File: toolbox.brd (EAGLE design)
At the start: 69.8 x 45 mm, 81 parts, among them IC1 PIC18F4XK22PT, IC3 78L05SMD, T1 BC847, U2 AD654JRZ, U3 ADUM7441ARQZ

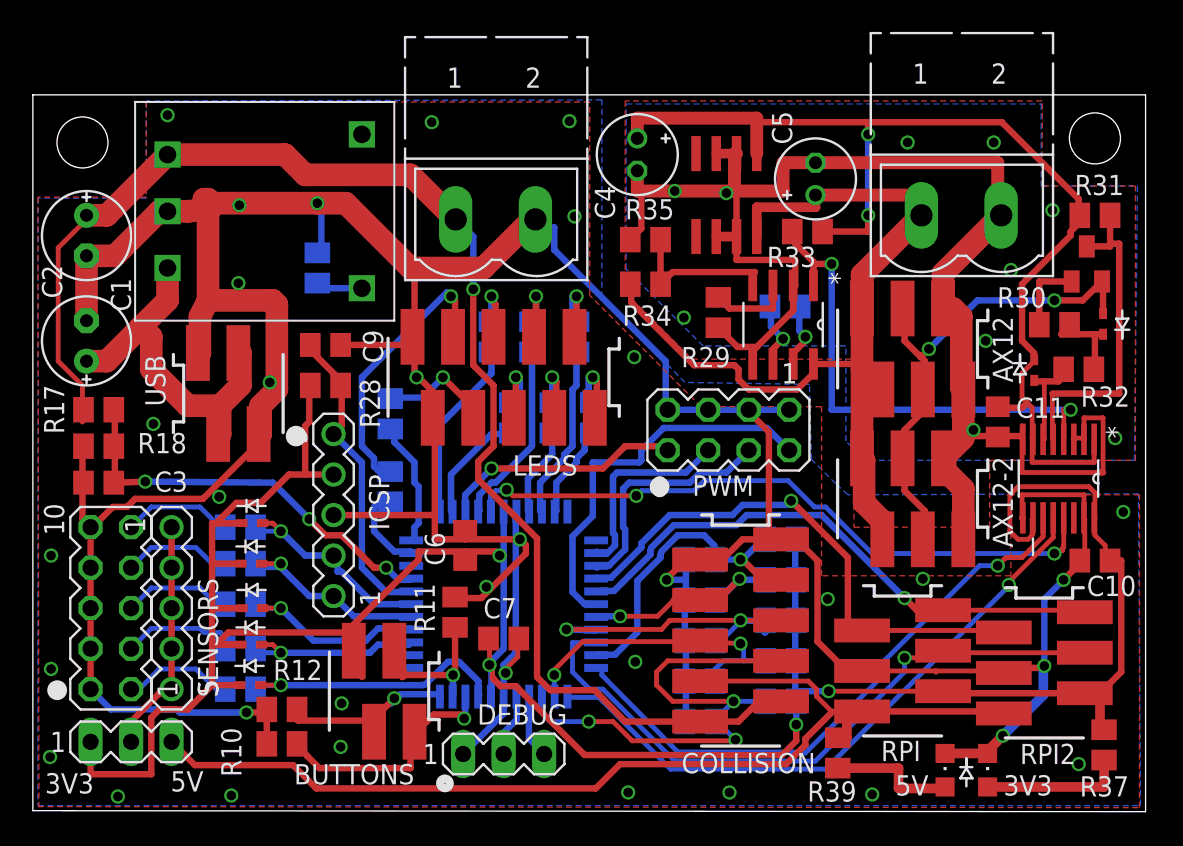
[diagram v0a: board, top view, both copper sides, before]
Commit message: added clipping circuit for collision sensors
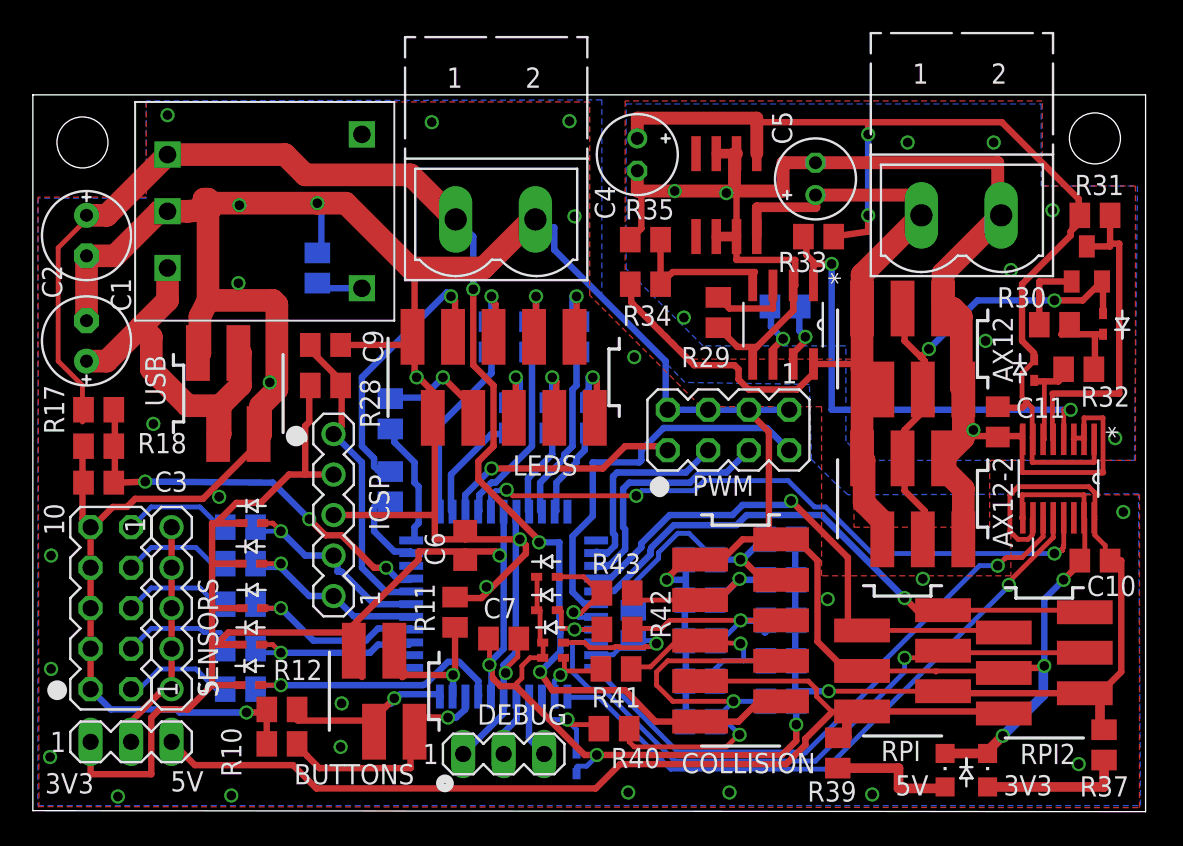
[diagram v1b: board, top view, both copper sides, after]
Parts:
- added D10, D11, D12, D8, D9: (no value), diode:SOD523
- added R40, R41, R42, R43, R44: 1k, rcl:M0805
- moved R33 0.77 mm to (49.3, 36.0)
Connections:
- new net N$66: D12.A, IC1.43, R44.1
- new net N$67: D8.A, IC1.3, R40.1
- new net N$69: D9.A, IC1.2, R41.1
- new net N$70: D10.A, IC1.41, R42.1
- new net N$71: D11.A, IC1.40, R43.1
- net N$41: now also R40.2; no longer IC1.3
- net N$42: now also R41.2; no longer IC1.2
- net N$43: now also R42.2; no longer IC1.41
- net N$44: now also R43.2; no longer IC1.40
- net N$45: now also R44.2; no longer IC1.43
- net VCC: now also D10.C, D11.C, D12.C, D8.C, D9.C
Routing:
- net VCC: track 171.8 -> 182.8 mm, vias 4 -> 5
- net N$66: track 0.00 -> 10.4 mm, vias 0 -> 1
- net N$67: track 0.00 -> 7.63 mm, vias 0 -> 1
- net N$71: track 0.00 -> 7.33 mm, vias 0 -> 1
- net N$42: track 19.7 -> 13.3 mm, vias 2 -> 1
- net N$43: track 23.0 -> 16.8 mm, vias 2 -> 1
- net N$69: track 0.00 -> 5.57 mm, vias 0 -> 1
- net N$70: track 0.00 -> 5.54 mm, vias 0 -> 1
- net N$41: track 34.2 -> 28.8 mm, vias 3 -> 2
- net N$45: track 20.9 -> 16.6 mm
- net N$44: track 14.1 -> 11.8 mm, vias 2 -> 1
- net N$35: track 90.1 -> 91.8 mm, vias 1 -> 3
- net N$68: track 69.6 -> 68.9 mm
- net N$63: track 31.5 -> 30.9 mm
- net GND: vias 35 -> 34

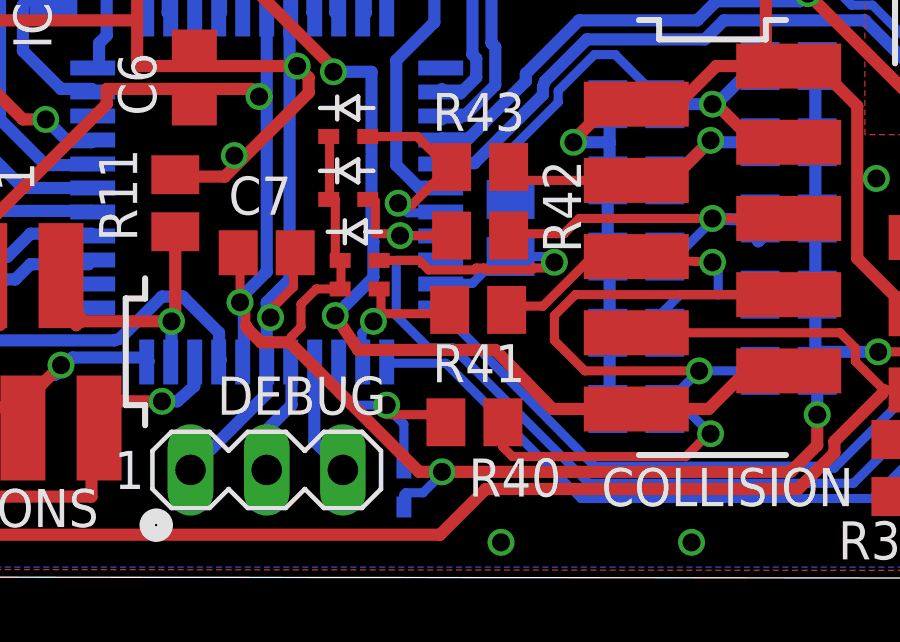
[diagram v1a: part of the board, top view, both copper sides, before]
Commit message: improved silk screen
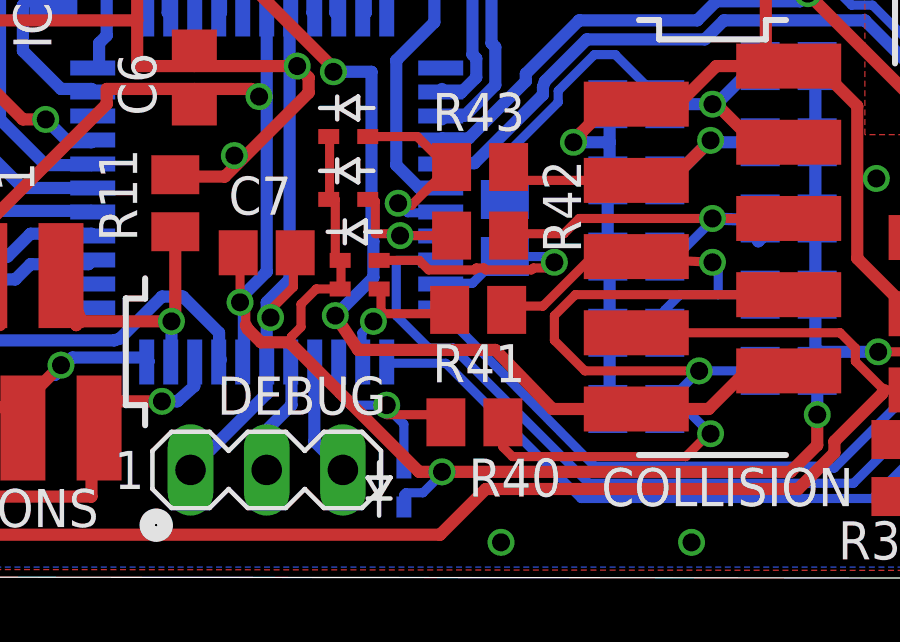
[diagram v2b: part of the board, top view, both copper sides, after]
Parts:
- moved R44 0.19 mm to (37.5, 11.6)
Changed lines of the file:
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@@
 <grid distance="0.0025" unitdist="inch" unit="mm" style="lines" multiple="1" display="no" altdistance="0.025" altunitdist="inch" altunit="inch"/>
 <layers>
-<layer number="1" name="Top" color="4" fill="1" visible="yes" active="yes"/>
+<layer number="1" name="Top" color="4" fill="1" visible="no" active="yes"/>
 <layer number="16" name="Bottom" color="1" fill="1" visible="yes" active="yes"/>
 <layer number="17" name="Pads" color="2" fill="1" visible="yes" active="yes"/>
@@
 <layer number="37" name="tTest" color="7" fill="1" visible="no" active="yes"/>
 <layer number="38" name="bTest" color="7" fill="1" visible="no" active="yes"/>
-<layer number="39" name="tKeepout" color="4" fill="11" visible="yes" active="yes"/>
+<layer number="39" name="tKeepout" color="4" fill="11" visible="no" active="yes"/>
 <layer number="40" name="bKeepout" color="1" fill="11" visible="yes" active="yes"/>
 <layer number="41" name="tRestrict" color="4" fill="10" visible="yes" active="yes"/>
@@
 <wire x1="32.5755" y1="15.621" x2="33.0835" y2="15.621" width="0.15" layer="25"/>
 <wire x1="31.877" y1="16.002" x2="31.877" y2="15.24" width="0.15" layer="25"/>
+<wire x1="33.274" y1="2.032" x2="33.274" y2="2.667" width="0.15" layer="25"/>
+<wire x1="33.274" y1="2.667" x2="32.893" y2="3.302" width="0.15" layer="25"/>
+<wire x1="32.893" y1="3.302" x2="33.274" y2="3.302" width="0.15" layer="25"/>
+<wire x1="33.274" y1="3.302" x2="33.655" y2="3.302" width="0.15" layer="25"/>
+<wire x1="33.655" y1="3.302" x2="33.274" y2="2.667" width="0.15" layer="25"/>
+<wire x1="33.274" y1="3.302" x2="33.274" y2="3.81" width="0.15" layer="25"/>
+<wire x1="32.893" y1="2.6035" x2="33.655" y2="2.6035" width="0.15" layer="25"/>
 </plain>
 <attributes>
@@
 </element>
 <element name="R14" library="rcl" package="M0805" value="2.2k" x="32.5755" y="24.638" smashed="yes" rot="MR270">
-<attribute name="NAME" x="33.147" y="22.7965" size="1.27" layer="26" rot="MR270"/>
+<attribute name="NAME" x="33.147" y="23.0505" size="1.27" layer="26" rot="MR270"/>
 </element>
 <element name="R15" library="rcl" package="M0805" value="2.2k" x="34.0995" y="29.718" smashed="yes" rot="MR270">
@@
 </element>
 <element name="R19" library="rcl" package="M0805" value="22k" x="41.8465" y="5.588" smashed="yes" rot="MR0">
-<attribute name="NAME" x="39.878" y="4.953" size="1.27" layer="26" rot="MR0"/>
+<attribute name="NAME" x="39.6875" y="4.699" size="1.27" layer="26" rot="MR0"/>
 </element>
 <element name="R2" library="rcl" package="M0805" value="2.2k" x="22.4155" y="24.892" smashed="yes" rot="MR90">
@@
 </element>
 <element name="R20" library="rcl" package="M0805" value="22k" x="41.8465" y="8.128" smashed="yes" rot="MR0">
-<attribute name="NAME" x="39.878" y="7.4295" size="1.27" layer="26" rot="MR0"/>
+<attribute name="NAME" x="39.6875" y="6.6675" size="1.27" layer="26" rot="MR0"/>
 </element>
 <element name="R21" library="rcl" package="M0805" value="22k" x="41.8465" y="10.668" smashed="yes" rot="MR0">
-<attribute name="NAME" x="39.878" y="10.033" size="1.27" layer="26" rot="MR0"/>
+<attribute name="NAME" x="39.6875" y="8.5725" size="1.27" layer="26" rot="MR0"/>
 </element>
 <element name="R23" library="rcl" package="M0805" value="22k" x="41.8465" y="13.208" smashed="yes" rot="MR0">
-<attribute name="NAME" x="39.8145" y="12.573" size="1.27" layer="26" rot="MR0"/>
+<attribute name="NAME" x="36.1315" y="15.24" size="1.27" layer="26" rot="MR180"/>
 </element>
 <element name="R24" library="rcl" package="M0805" value="22k" x="46.9265" y="14.478" smashed="yes" rot="MR0">
@@
 </element>
 <element name="R22" library="rcl" package="M0805" value="22k" x="41.8465" y="15.748" smashed="yes" rot="MR0">
-<attribute name="NAME" x="39.8145" y="14.986" size="1.27" layer="26" rot="MR0"/>
+<attribute name="NAME" x="43.3705" y="17.0815" size="1.27" layer="26" rot="MR0"/>
 </element>
 <element name="R36" library="rcl" package="M0805" value="22k" x="46.9265" y="17.018" smashed="yes" rot="MR0">
@@
 <attribute name="NAME" x="35.052" y="14.859" size="1.27" layer="25"/>
 </element>
-<element name="R44" library="rcl" package="M0805" value="1k" x="37.6555" y="11.6205" smashed="yes" rot="MR90">
-<attribute name="NAME" x="38.9255" y="10.3505" size="1.27" layer="26" rot="MR90"/>
-<attribute name="VALUE" x="35.1155" y="10.3505" size="1.27" layer="28" rot="MR90"/>
+<element name="R44" library="rcl" package="M0805" value="1k" x="37.465" y="11.6205" smashed="yes" rot="MR90">
+<attribute name="NAME" x="38.481" y="10.7315" size="1.27" layer="26" rot="MR90"/>
 </element>
 <element name="D8" library="diode" package="SOD523" value="" x="34.0995" y="2.921" smashed="yes" rot="MR90">
-<attribute name="NAME" x="34.7345" y="2.286" size="1.27" layer="26" rot="MR90"/>
+<attribute name="NAME" x="36.957" y="1.5875" size="1.27" layer="26" rot="MR0"/>
 <attribute name="VALUE" x="32.1945" y="2.286" size="1.27" layer="28" rot="MR90"/>
 </element>
@@
 <wire x1="37.6555" y1="12.573" x2="37.338" y2="12.573" width="0.3048" layer="16"/>
 <wire x1="42.672" y1="15.875" x2="42.7965" y2="15.748" width="0.3048" layer="16"/>
-<wire x1="37.6555" y1="12.573" x2="37.6555" y2="12.5705" width="0.3048" layer="16"/>
+<wire x1="37.6555" y1="12.573" x2="37.465" y2="12.5705" width="0.3048" layer="16"/>
 </signal>
 <signal name="N$40">
@@
 <wire x1="36.3855" y1="9.779" x2="37.2745" y2="10.668" width="0.3048" layer="16"/>
 <wire x1="35.3695" y1="9.779" x2="36.3855" y2="9.779" width="0.3048" layer="16"/>
-<wire x1="37.6555" y1="10.668" x2="37.6555" y2="10.6705" width="0.3048" layer="16"/>
+<wire x1="37.6555" y1="10.668" x2="37.465" y2="10.6705" width="0.3048" layer="16"/>
 <wire x1="35.3695" y1="9.779" x2="35.3275" y2="9.754" width="0.3048" layer="16"/>
 <contactref element="D12" pad="A"/>
@@
 <wire x1="38.7985" y1="10.668" x2="38.989" y2="10.4775" width="0.3048" layer="16"/>
 <wire x1="37.7825" y1="10.668" x2="38.7985" y2="10.668" width="0.3048" layer="16"/>
-<wire x1="37.7825" y1="10.668" x2="37.6555" y2="10.6705" width="0.3048" layer="16"/>
+<wire x1="37.7825" y1="10.668" x2="37.465" y2="10.6705" width="0.3048" layer="16"/>
 <via x="39.116" y="10.4775" extent="1-16" drill="0.6"/>
 </signal>

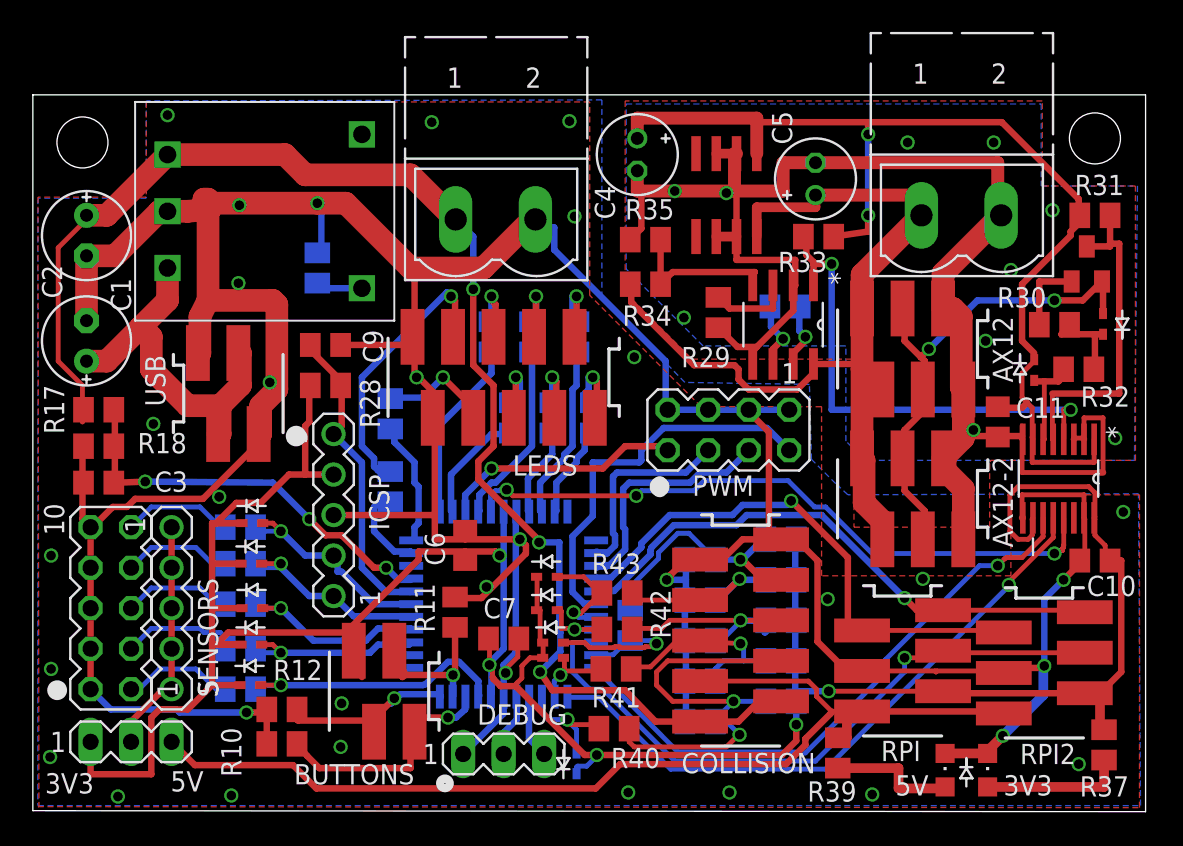
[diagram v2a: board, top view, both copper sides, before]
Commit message: circuit checked, added filtering capacitor and fixed a last clearance error
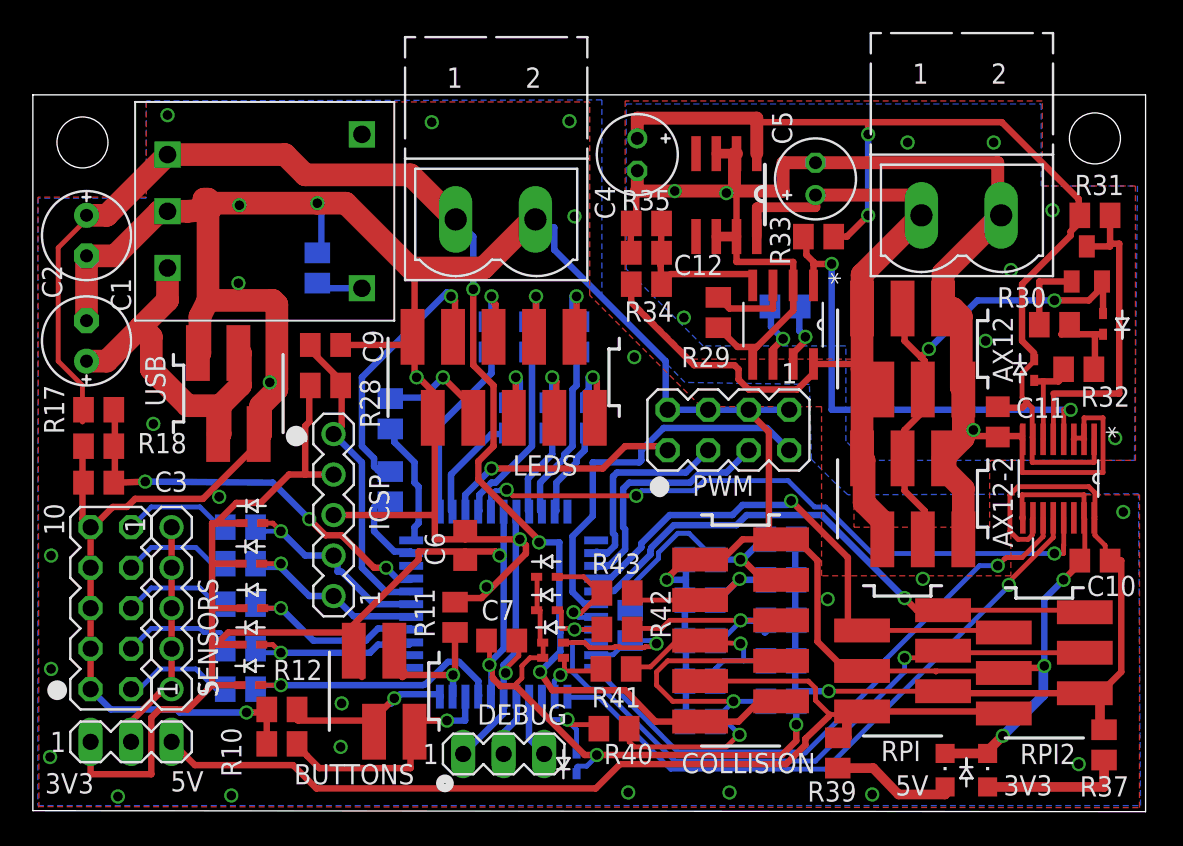
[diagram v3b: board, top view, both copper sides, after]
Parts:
- added C12: 100n, rcl:C0805
- moved R35 1.02 mm to (38.5, 36.8)
- moved R11 0.32 mm to (26.5, 12.1)
- moved C7 0.18 mm to (29.4, 10.7)
- moved R34 0.06 mm to (38.5, 33.0)
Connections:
- net GND_MOTOR: now also C12.2
- net N$49: now also C12.1
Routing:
- net GND_MOTOR: track 100.8 -> 102.4 mm
- net N$49: track 9.91 -> 11.3 mm
